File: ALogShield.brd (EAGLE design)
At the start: 53.3 x 78.5 mm, 34 parts, among them U1 DS3231MZ/V+T

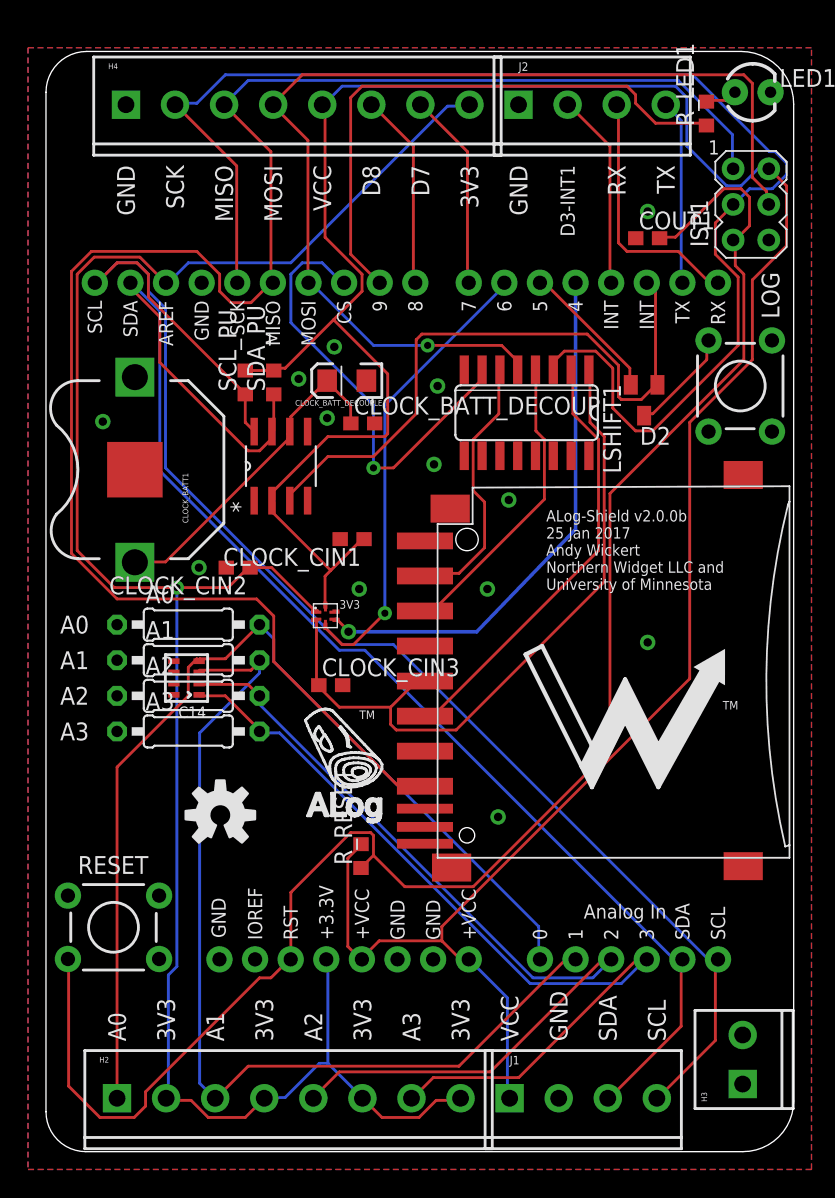
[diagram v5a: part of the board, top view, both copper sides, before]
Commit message: More space for Rref; smaller vias
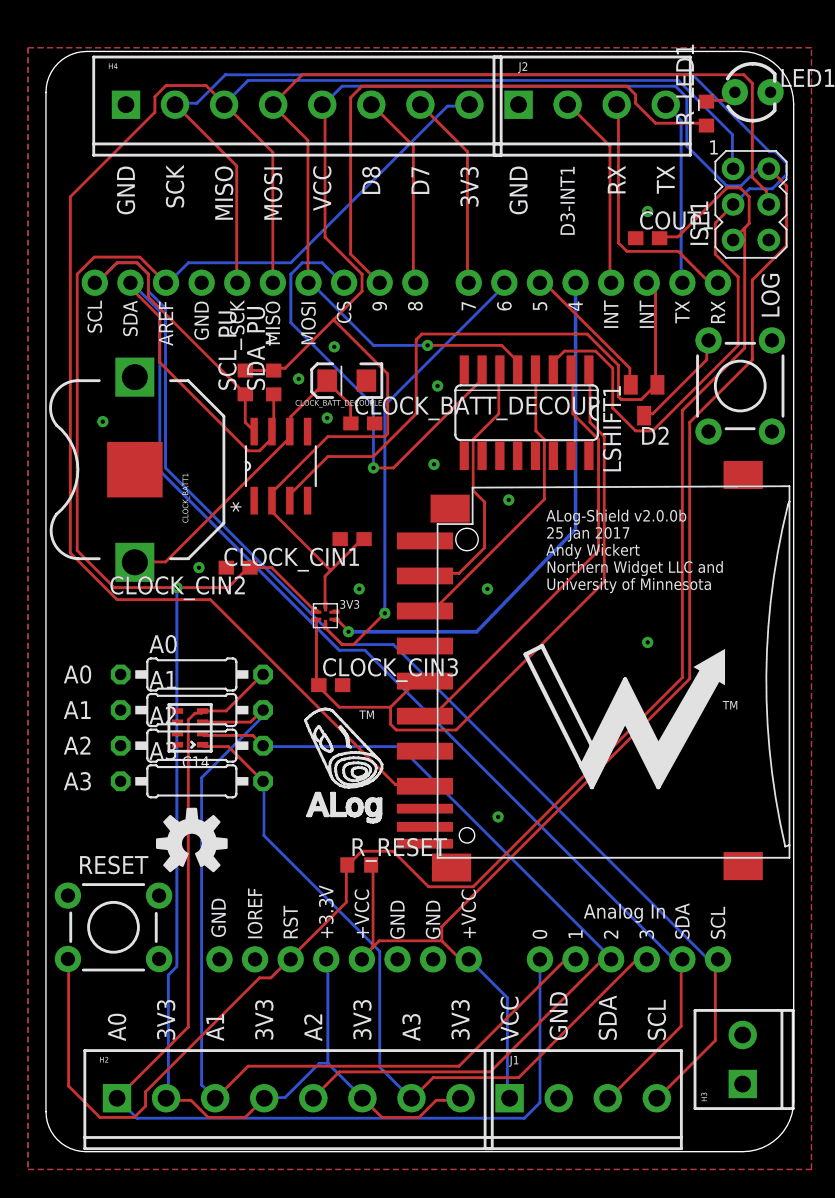
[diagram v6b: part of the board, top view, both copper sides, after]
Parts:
- moved A1 3.57 mm to (10.4, 31.5)
- moved A2 3.57 mm to (10.4, 29.0)
- moved A3 3.57 mm to (10.4, 26.4)
- moved A0 3.57 mm to (10.4, 34.0)
- moved C14 3.57 mm to (10.3, 30.2)
- moved LOGO2 2.87 mm to (10.4, 22.0)
- moved R_RESET 0.65 mm to (22.4, 20.4), turned to 0 degrees
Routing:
- net A3: track 62.1 -> 53.3 mm
- net A0: track 71.5 -> 77.2 mm
- net RESET: track 120.5 -> 116.6 mm
- net A1: track 68.0 -> 64.4 mm
- net VCC: track 191.0 -> 187.9 mm
- net A2: track 64.4 -> 61.2 mm
- net DO: track 127.1 -> 128.4 mm

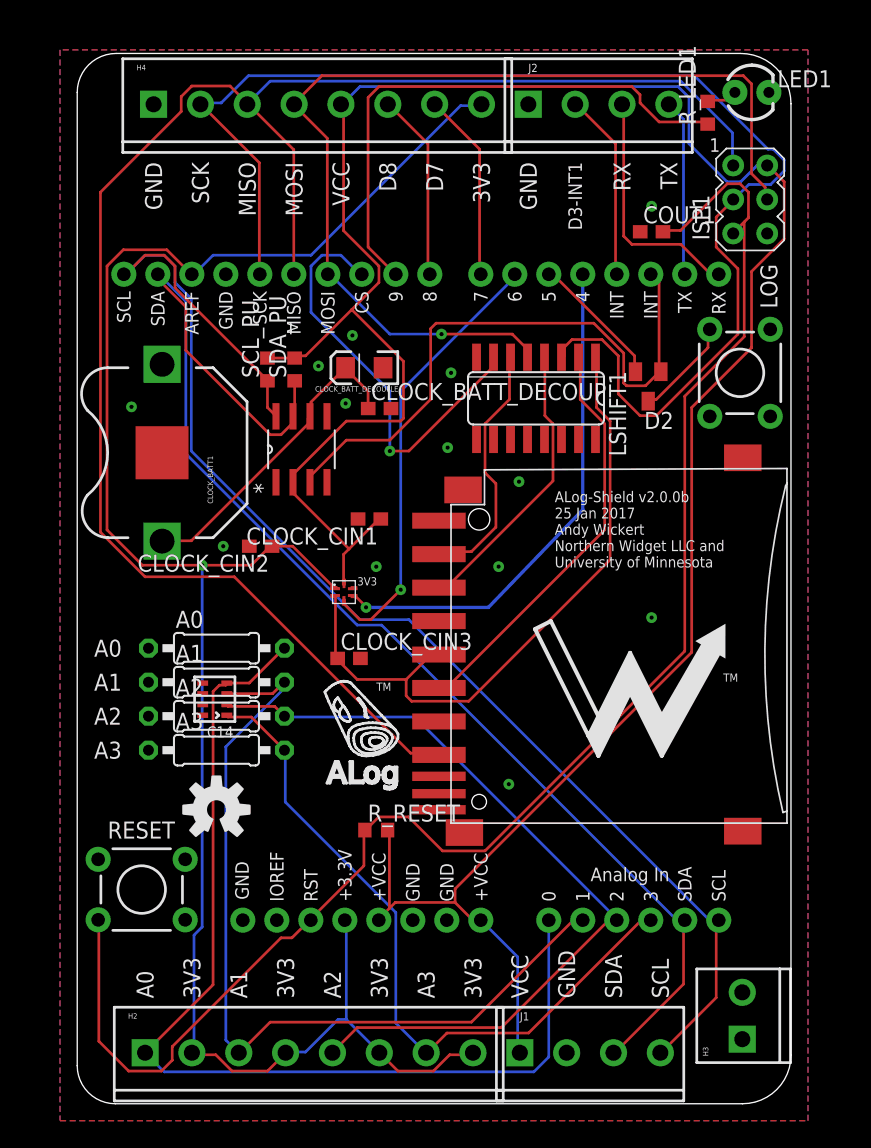
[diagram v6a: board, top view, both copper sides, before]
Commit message: Remove JST power connector; move buttons to symmetrical places
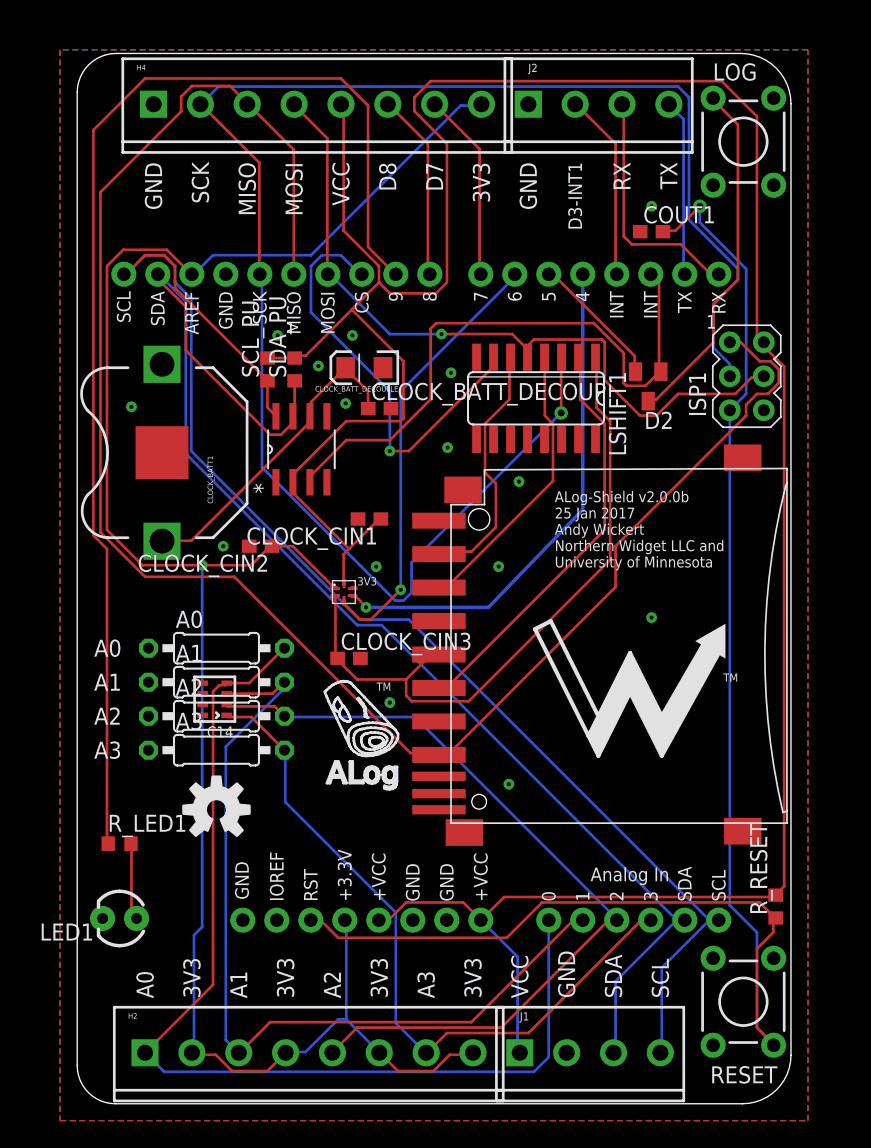
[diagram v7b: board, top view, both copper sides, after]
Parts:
- removed H3: (no value), SparkFun-Connectors:SCREWTERMINAL-3.5MM-2
- moved LED1 77.7 mm to (3.17, 13.8), turned to 180 degrees
- moved R_LED1 70.1 mm to (3.17, 19.4), turned to 0 degrees
- moved RESET 45.7 mm to (49.8, 7.62), turned to 90 degrees
- moved R_RESET 30.4 mm to (52.2, 14.7), turned to 90 degrees
- moved LOG 17.3 mm to (49.8, 71.9)
- moved ISP1 13.2 mm to (50.0, 54.4)
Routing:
- net D9-LED: track 41.3 -> 90.2 mm
- net CLK: track 99.0 -> 127.9 mm, vias 0 -> 1
- net DI: track 76.1 -> 55.6 mm
- net VCC: track 187.9 -> 208.3 mm
- net N$11: track 7.62 -> 26.5 mm
- net DO: track 128.4 -> 132.0 mm
- net LED+1: track 2.34 -> 5.75 mm
- net RESET: track 116.6 -> 117.1 mm, vias 0 -> 1
- net GND: track 0.07 -> 0.36 mm, vias 13 -> 15

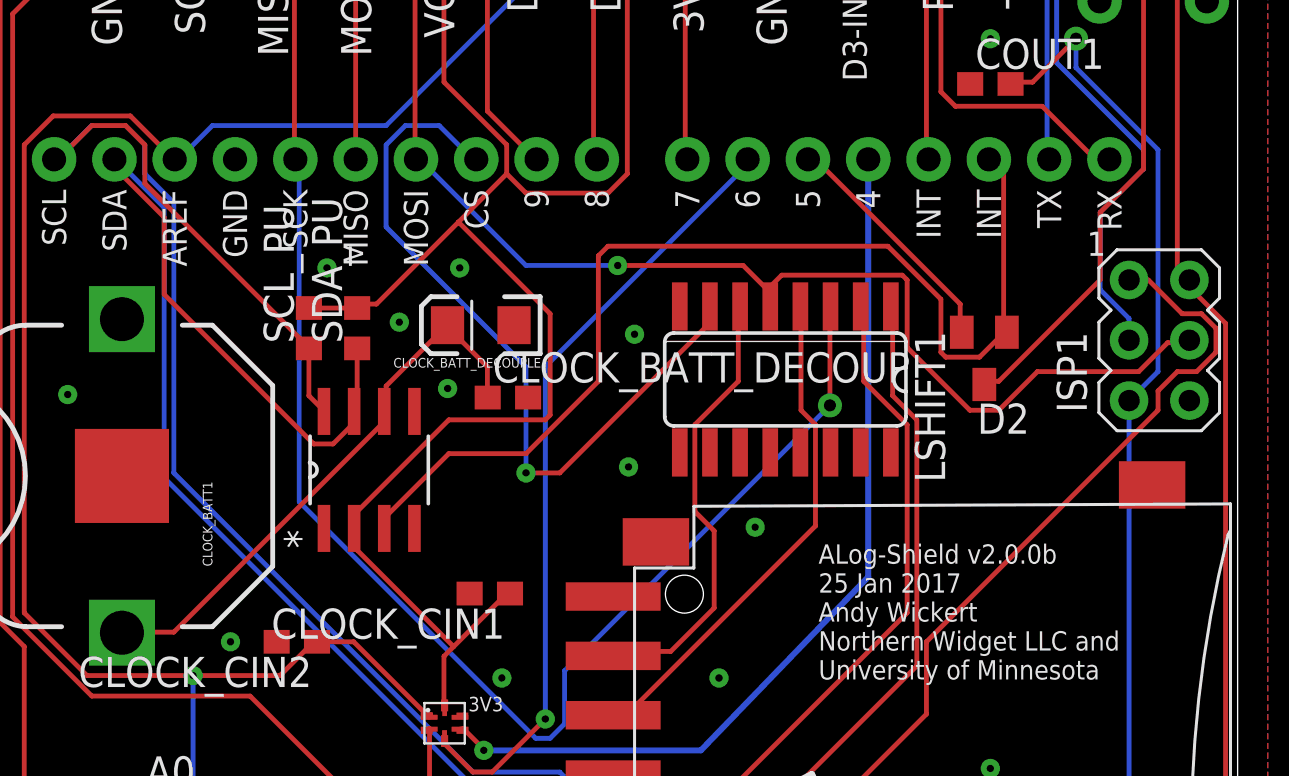
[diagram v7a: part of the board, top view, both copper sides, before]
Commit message: Use our in-stock 3.3k-ohm pull-up resistor array, even if only 2/4 in use
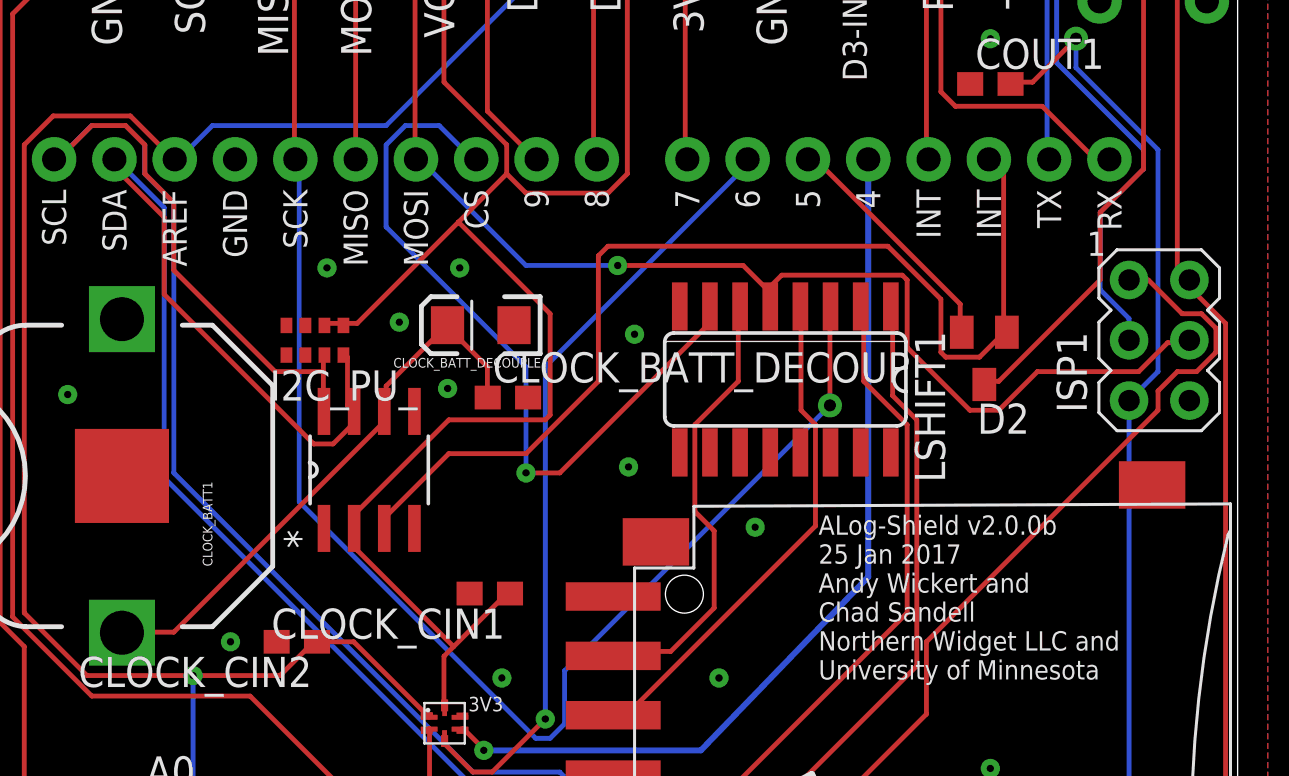
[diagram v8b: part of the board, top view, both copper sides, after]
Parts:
- removed SCL_PU, SDA_PU: 10k, rcl:R0603
- added I2C_PU_: 3.3K, resistor-dil:0603-ARC
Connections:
- net SCL: now also I2C_PU_.3; no longer SCL_PU.1
- net SDA: now also I2C_PU_.4; no longer SDA_PU.1
- net VCC: now also I2C_PU_.5, I2C_PU_.6; no longer SCL_PU.2, SDA_PU.2
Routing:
- net SCL: track 104.3 -> 106.2 mm
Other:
- board text added: "ALog-Shield v2.0.0b 25 Jan 2017 Andy Wickert and Chad Sandell Northern Widget LLC and University of Minnesota"
- board text removed: "ALog-Shield v2.0.0b 25 Jan 2017 Andy Wickert Northern Widget LLC and University of Minnesota"
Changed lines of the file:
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@@
 <text x="35.687" y="40.0685" size="0.8128" layer="21">ALog-Shield v2.0.0b
 25 Jan 2017
-Andy Wickert
+Andy Wickert and
+Chad Sandell
 Northern Widget LLC and
 University of Minnesota</text>
@@
 <attribute name="PROD_ID" value="2xCONN-08399" x="33.715" y="74.676" size="1.778" layer="27" display="off"/>
 </element>
-<element name="SCL_PU" library="rcl" package="R0603" value="10k" x="14.224" y="54.864" rot="R90"/>
-<element name="SDA_PU" library="rcl" package="R0603" value="10k" x="16.256" y="54.864" rot="R90"/>
+<element name="I2C_PU_" library="resistor-dil" package="0603-ARC" value="3.3K" x="14.478" y="54.356">
+<attribute name="MPN" value="" x="-3.556" y="32.512" size="1.778" layer="27" display="off"/>
+<attribute name="OC_NEWARK" value="unknown" x="-3.556" y="32.512" size="1.778" layer="27" display="off"/>
+<attribute name="MF" value="" x="-3.556" y="32.512" size="1.778" layer="27" display="off"/>
+<attribute name="OC_FARNELL" value="unknown" x="-3.556" y="32.512" size="1.778" layer="27" display="off"/>
+</element>
 </elements>
 <signals>
@@
 <contactref element="U1" pad="2"/>
 <contactref element="H4" pad="5"/>
-<contactref element="SCL_PU" pad="2"/>
-<contactref element="SDA_PU" pad="2"/>
 <wire x1="32.9184" y1="10.9728" x2="32.9184" y2="3.8608" width="0.2032" layer="16"/>
 <wire x1="30.2768" y1="13.6144" x2="32.9184" y2="10.9728" width="0.2032" layer="16"/>
@@
 <wire x1="16.256" y1="46.3296" x2="16.256" y2="45.5168" width="0.2032" layer="1"/>
 <wire x1="16.256" y1="46.3296" x2="16.129" y2="46.4312" width="0.2032" layer="1"/>
-<wire x1="14.224" y1="55.714" x2="16.256" y2="55.714" width="0.2032" layer="1"/>
-<wire x1="17.0688" y1="55.88" x2="16.256" y2="55.88" width="0.2032" layer="1"/>
-<wire x1="22.5552" y1="61.3664" x2="20.5232" y2="59.3344" width="0.2032" layer="1"/>
-<wire x1="20.5232" y1="59.3344" x2="17.0688" y2="55.88" width="0.2032" layer="1"/>
-<wire x1="22.5552" y1="62.5856" x2="22.5552" y2="61.3664" width="0.2032" layer="1"/>
-<wire x1="19.9136" y1="65.2272" x2="22.5552" y2="62.5856" width="0.2032" layer="1"/>
-<wire x1="19.9136" y1="74.5744" x2="19.9136" y2="65.2272" width="0.2032" layer="1"/>
-<wire x1="16.256" y1="55.88" x2="16.256" y2="55.714" width="0.2032" layer="1"/>
-<wire x1="19.9136" y1="74.5744" x2="19.715" y2="74.676" width="0.2032" layer="1"/>
-<wire x1="16.256" y1="47.1424" x2="16.256" y2="46.5328" width="0.2032" layer="1"/>
-<wire x1="20.1168" y1="51.0032" x2="16.256" y2="47.1424" width="0.2032" layer="1"/>
-<wire x1="24.1808" y1="51.0032" x2="20.1168" y2="51.0032" width="0.2032" layer="1"/>
-<wire x1="24.384" y1="51.2064" x2="24.1808" y2="51.0032" width="0.2032" layer="1"/>
-<wire x1="24.384" y1="55.4736" x2="24.384" y2="51.2064" width="0.2032" layer="1"/>
-<wire x1="20.5232" y1="59.3344" x2="24.384" y2="55.4736" width="0.2032" layer="1"/>
-<wire x1="16.256" y1="46.5328" x2="16.129" y2="46.4312" width="0.2032" layer="1"/>
 <wire x1="31.9024" y1="15.4432" x2="52.0192" y2="15.4432" width="0.2032" layer="1"/>
 <wire x1="30.2768" y1="13.8176" x2="31.9024" y2="15.4432" width="0.2032" layer="1"/>
@@
 <wire x1="22.5552" y1="13.8176" x2="22.5425" y2="13.716" width="0.2032" layer="1"/>
 <wire x1="30.0736" y1="13.8176" x2="30.1625" y2="13.716" width="0.2032" layer="1"/>
+<contactref element="I2C_PU_" pad="6"/>
+<contactref element="I2C_PU_" pad="5"/>
+<wire x1="15.6464" y1="55.0672" x2="15.0368" y2="55.0672" width="0.2032" layer="1"/>
+<wire x1="15.0368" y1="55.0672" x2="14.878" y2="54.981" width="0.2032" layer="1"/>
+<wire x1="15.6464" y1="55.0672" x2="15.678" y2="54.981" width="0.2032" layer="1"/>
+<wire x1="16.256" y1="55.0672" x2="15.8496" y2="55.0672" width="0.2032" layer="1"/>
+<wire x1="22.5552" y1="61.3664" x2="20.5232" y2="59.3344" width="0.2032" layer="1"/>
+<wire x1="20.5232" y1="59.3344" x2="16.256" y2="55.0672" width="0.2032" layer="1"/>
+<wire x1="22.5552" y1="62.5856" x2="22.5552" y2="61.3664" width="0.2032" layer="1"/>
+<wire x1="19.9136" y1="65.2272" x2="22.5552" y2="62.5856" width="0.2032" layer="1"/>
+<wire x1="19.9136" y1="74.5744" x2="19.9136" y2="65.2272" width="0.2032" layer="1"/>
+<wire x1="15.8496" y1="55.0672" x2="15.678" y2="54.981" width="0.2032" layer="1"/>
+<wire x1="19.9136" y1="74.5744" x2="19.715" y2="74.676" width="0.2032" layer="1"/>
+<wire x1="16.256" y1="47.1424" x2="16.256" y2="46.5328" width="0.2032" layer="1"/>
+<wire x1="20.1168" y1="51.0032" x2="16.256" y2="47.1424" width="0.2032" layer="1"/>
+<wire x1="24.1808" y1="51.0032" x2="20.1168" y2="51.0032" width="0.2032" layer="1"/>
+<wire x1="24.384" y1="51.2064" x2="24.1808" y2="51.0032" width="0.2032" layer="1"/>
+<wire x1="24.384" y1="55.4736" x2="24.384" y2="51.2064" width="0.2032" layer="1"/>
+<wire x1="20.5232" y1="59.3344" x2="24.384" y2="55.4736" width="0.2032" layer="1"/>
+<wire x1="16.256" y1="46.5328" x2="16.129" y2="46.4312" width="0.2032" layer="1"/>
 <wire x1="23.368" y1="60.5536" x2="22.5552" y2="61.3664" width="0.2032" layer="1"/>
 <wire x1="26.8224" y1="60.5536" x2="23.368" y2="60.5536" width="0.2032" layer="1"/>
@@
 <contactref element="J1" pad="4"/>
 <contactref element="U1" pad="8"/>
-<contactref element="SCL_PU" pad="1"/>
-<wire x1="14.224" y1="52.0192" x2="14.224" y2="54.014" width="0.2032" layer="1"/>
-<wire x1="14.8336" y1="51.4096" x2="14.224" y2="52.0192" width="0.2032" layer="1"/>
-<wire x1="14.8336" y1="51.4096" x2="14.859" y2="51.3588" width="0.2032" layer="1"/>
-<wire x1="7.3152" y1="60.96" x2="14.224" y2="54.0512" width="0.2032" layer="1"/>
-<wire x1="7.3152" y1="62.5856" x2="7.3152" y2="60.96" width="0.2032" layer="1"/>
-<wire x1="6.5024" y1="63.3984" x2="7.3152" y2="62.5856" width="0.2032" layer="1"/>
-<wire x1="5.08" y1="63.3984" x2="6.5024" y2="63.3984" width="0.2032" layer="1"/>
-<wire x1="3.6576" y1="61.976" x2="5.08" y2="63.3984" width="0.2032" layer="1"/>
-<wire x1="14.224" y1="54.0512" x2="14.224" y2="54.014" width="0.2032" layer="1"/>
-<wire x1="3.6576" y1="61.976" x2="3.4925" y2="61.976" width="0.2032" layer="1"/>
 <wire x1="47.1424" y1="13.8176" x2="47.3456" y2="13.8176" width="0.2032" layer="16"/>
 <wire x1="47.3456" y1="13.8176" x2="47.752" y2="13.8176" width="0.2032" layer="16"/>
@@
 <wire x1="43.688" y1="3.8608" x2="43.58" y2="3.81" width="0.2032" layer="16"/>
 <wire x1="47.3456" y1="13.8176" x2="47.9425" y2="13.716" width="0.2032" layer="16"/>
+<contactref element="I2C_PU_" pad="3"/>
+<wire x1="14.8336" y1="51.4096" x2="14.8336" y2="53.0352" width="0.2032" layer="1"/>
+<wire x1="14.8336" y1="53.0352" x2="14.8336" y2="53.6448" width="0.2032" layer="1"/>
+<wire x1="14.8336" y1="53.6448" x2="14.878" y2="53.731" width="0.2032" layer="1"/>
+<wire x1="14.8336" y1="51.4096" x2="14.859" y2="51.3588" width="0.2032" layer="1"/>
+<wire x1="12.8016" y1="53.0352" x2="14.8336" y2="53.0352" width="0.2032" layer="1"/>
+<wire x1="8.5344" y1="57.3024" x2="12.8016" y2="53.0352" width="0.2032" layer="1"/>
+<wire x1="8.5344" y1="60.1472" x2="8.5344" y2="57.3024" width="0.2032" layer="1"/>
+<wire x1="7.3152" y1="61.3664" x2="8.5344" y2="60.1472" width="0.2032" layer="1"/>
+<wire x1="7.3152" y1="62.5856" x2="7.3152" y2="61.3664" width="0.2032" layer="1"/>
+<wire x1="6.5024" y1="63.3984" x2="7.3152" y2="62.5856" width="0.2032" layer="1"/>
+<wire x1="5.08" y1="63.3984" x2="6.5024" y2="63.3984" width="0.2032" layer="1"/>
+<wire x1="3.6576" y1="61.976" x2="5.08" y2="63.3984" width="0.2032" layer="1"/>
+<wire x1="3.6576" y1="61.976" x2="3.4925" y2="61.976" width="0.2032" layer="1"/>
 </signal>
 <signal name="SDA">
@@
 <contactref element="J1" pad="3"/>
 <contactref element="U1" pad="7"/>
-<contactref element="SDA_PU" pad="1"/>
-<wire x1="16.256" y1="51.4096" x2="16.256" y2="54.014" width="0.2032" layer="1"/>
 <wire x1="16.256" y1="51.4096" x2="16.129" y2="51.3588" width="0.2032" layer="1"/>
 <wire x1="16.0528" y1="50.8" x2="16.0528" y2="51.2064" width="0.2032" layer="1"/>
@@
 <wire x1="40.2336" y1="3.8608" x2="40.08" y2="3.81" width="0.2032" layer="16"/>
 <wire x1="44.9072" y1="13.8176" x2="45.4025" y2="13.716" width="0.2032" layer="16"/>
+<contactref element="I2C_PU_" pad="4"/>
+<wire x1="15.8496" y1="51.6128" x2="15.8496" y2="53.6448" width="0.2032" layer="1"/>
+<wire x1="16.0528" y1="51.4096" x2="15.8496" y2="51.6128" width="0.2032" layer="1"/>
+<wire x1="15.8496" y1="53.6448" x2="15.678" y2="53.731" width="0.2032" layer="1"/>
+<wire x1="16.0528" y1="51.4096" x2="16.129" y2="51.3588" width="0.2032" layer="1"/>
 </signal>
 <signal name="INT0">
